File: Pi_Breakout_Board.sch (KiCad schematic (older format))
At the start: 74 parts, among them J1 Raspberry_Pi_2_3, J2 Conn_02x04_Odd_Even heater he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, J3 Conn_02x08_Odd_Even thermisto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, J4 Screw_Terminal_01x02, J5 Conn_01x08_Male, J6 Conn_01x08_Male, J7 Conn_01x05_Male uart breakout, Q1 Q_NMOS_GDSD, Q2 Q_NMOS_GDSD, Q3 Q_NMOS_GDSD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

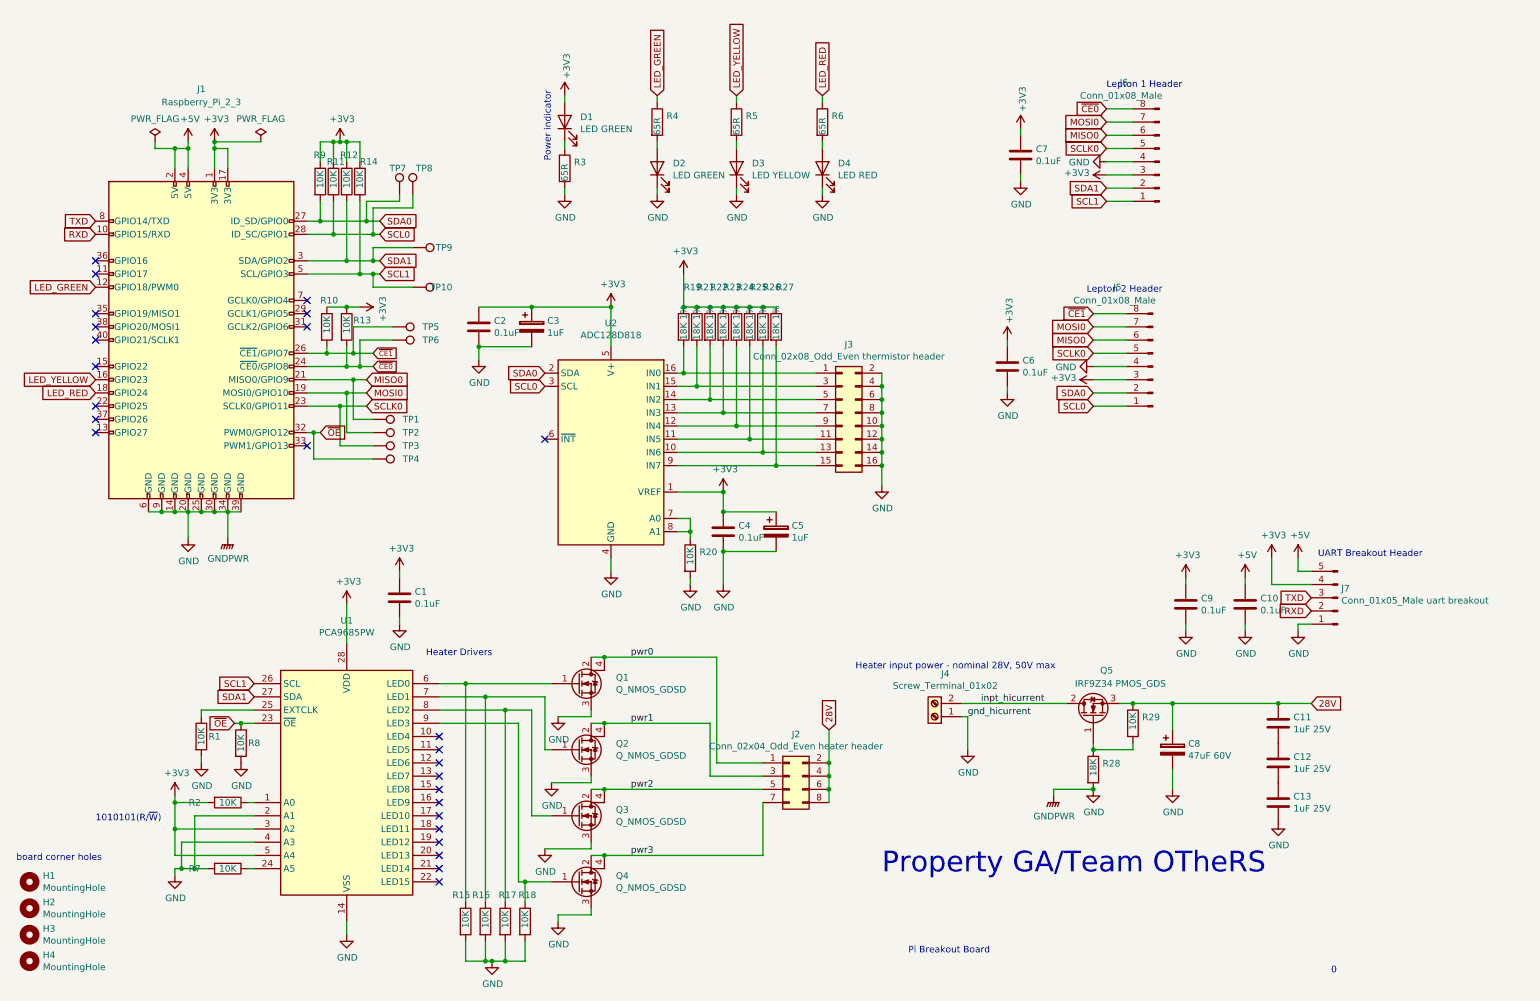
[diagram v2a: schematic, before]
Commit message: remove MOSI line (unused)
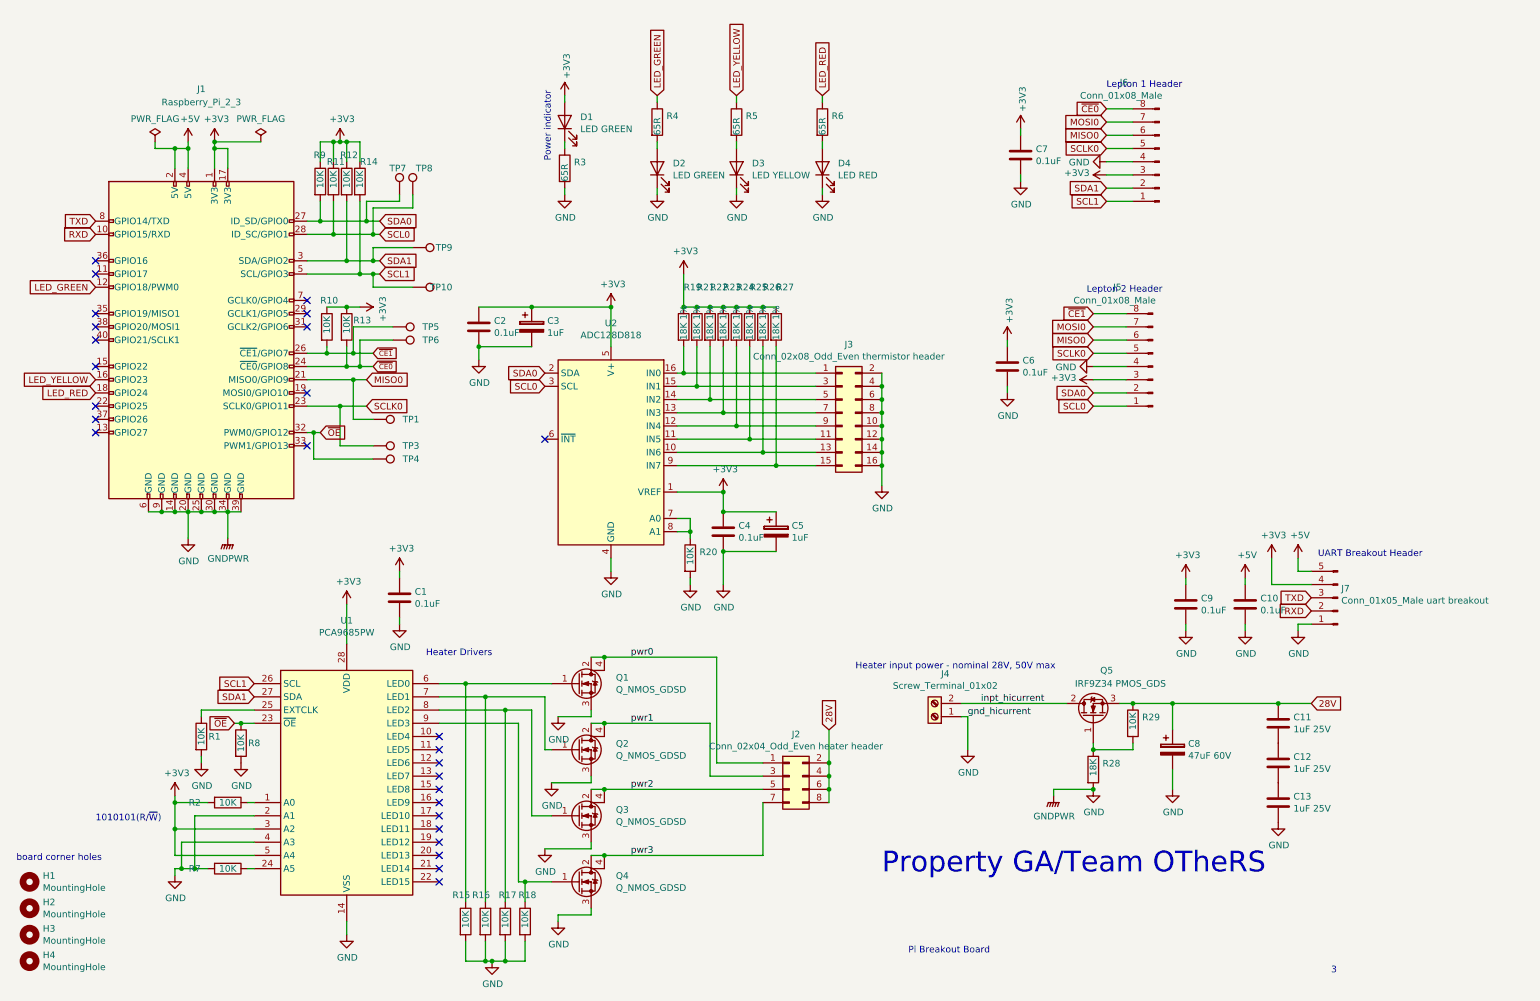
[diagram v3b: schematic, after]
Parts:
- removed TP2: TestPoint, TestPoint:TestPoint_Pad_D2.0mm, symbol Connector:TestPoint
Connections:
- net MOSI0: no longer J1.19 (MOSI0/GPIO10)
- no-connect marks 26 -> 27
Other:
- note added: "3"
- note removed: "0"
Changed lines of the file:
@@
 Text GLabel 3300 3150 2    50   Input ~ 0
 MISO0
-Text GLabel 3300 3250 2    50   Input ~ 0
-MOSI0
 Text GLabel 3300 3350 2    50   Input ~ 0
 SCLK0
@@
 Pi Breakout Board
 Text Notes 10600 7650 0    50   ~ 0
-0
+3
 Text Label 5300 5750 0    50   ~ 0
 pwr1
@@
 	2850 3150 3200 3150
 Wire Wire Line
-	2850 3250 3150 3250
-Wire Wire Line
 	2850 3350 3100 3350
 $Comp
@@
 $EndComp
 $Comp
-L Connector:TestPoint TP2
-U 1 1 5C84A9FB
-P 3350 3550
-F 0 "TP2" V 3350 3900 50  0000 R CNN
-F 1 "TestPoint" H 3292 3668 50  0001 R CNN
-F 2 "TestPoint:TestPoint_Pad_D2.0mm" H 3550 3550 50  0001 C CNN
-F 3 "~" H 3550 3550 50  0001 C CNN
-	1    3350 3550
-	0    1    1    0
-$EndComp
-$Comp
 L Connector:TestPoint TP3
 U 1 1 5C84AA97
@@
 	3200 3150 3300 3150
 Wire Wire Line
-	3350 3550 3150 3550
-Wire Wire Line
-	3150 3550 3150 3250
-Connection ~ 3150 3250
-Wire Wire Line
-	3150 3250 3300 3250
-Wire Wire Line
 	3350 3650 3100 3650
 Wire Wire Line
@@
 NoConn ~ 1250 2750
 NoConn ~ 1250 2250
+NoConn ~ 2850 3250
 $EndSCHEMATC

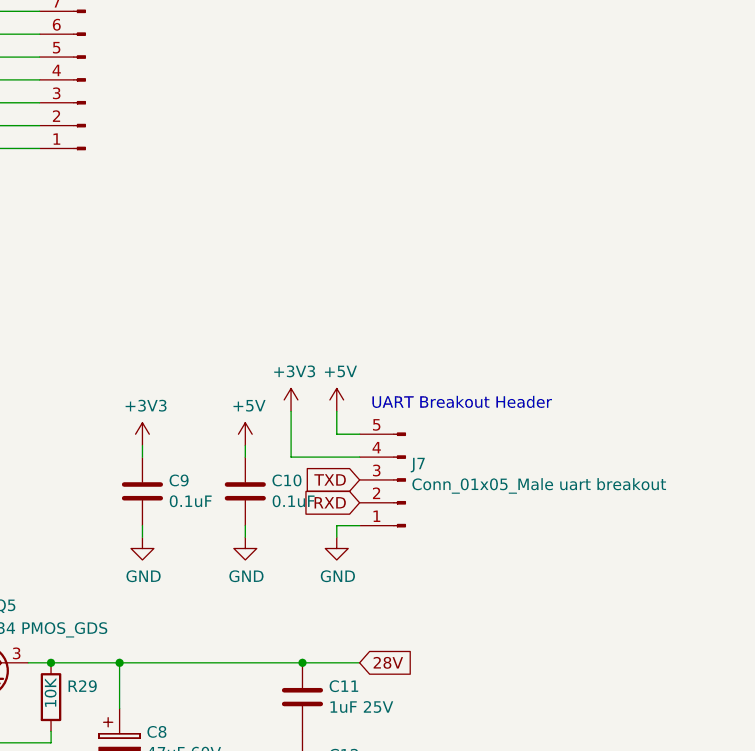
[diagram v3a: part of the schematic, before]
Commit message: Add +5V power header
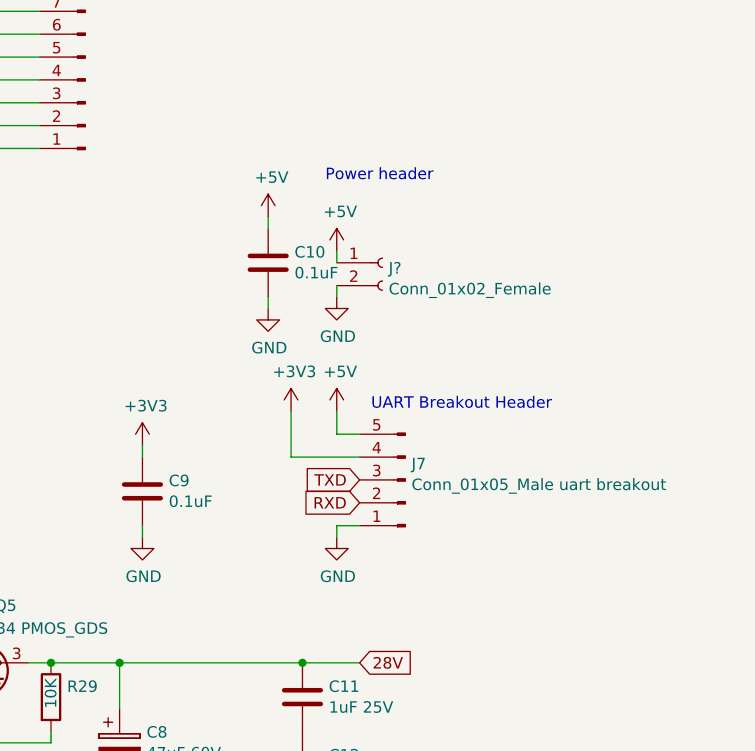
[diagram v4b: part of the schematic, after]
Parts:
- added J?: Conn_01x02_Female, symbol Connector:Conn_01x02_Female
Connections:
- net +5V: now also J?.1 (Pin_1)
- net GND: now also J?.2 (Pin_2)
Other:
- note added: "Power header"
- moved on the sheet: C10
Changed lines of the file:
@@
 L power:+5V #PWR046
 U 1 1 5C584F51
-P 10350 4500
-F 0 "#PWR046" H 10350 4350 50  0001 C CNN
-F 1 "+5V" H 10365 4673 50  0000 C CNN
-F 2 "" H 10350 4500 50  0001 C CNN
-F 3 "" H 10350 4500 50  0001 C CNN
-	1    10350 4500
+P 10350 3800
+F 0 "#PWR046" H 10350 3650 50  0001 C CNN
+F 1 "+5V" H 10365 3973 50  0000 C CNN
+F 2 "" H 10350 3800 50  0001 C CNN
+F 3 "" H 10350 3800 50  0001 C CNN
+	1    10350 3800
 	1    0    0    -1
 $EndComp
@@
 L Device:C C10
 U 1 1 5C6E7D8F
-P 9950 4850
-F 0 "C10" H 10065 4896 50  0000 L CNN
-F 1 "0.1uF" H 10065 4805 50  0000 L CNN
-F 2 "Capacitor_SMD:C_1210_3225Metric_Pad1.42x2.65mm_HandSolder" H 9988 4700 50  0001 C CNN
-F 3 "~" H 9950 4850 50  0001 C CNN
-	1    9950 4850
-	1    0    0    -1
-$EndComp
-Wire Wire Line
-	9950 4650 9950 4700
+P 10050 3850
+F 0 "C10" H 10165 3896 50  0000 L CNN
+F 1 "0.1uF" H 10165 3805 50  0000 L CNN
+F 2 "Capacitor_SMD:C_1210_3225Metric_Pad1.42x2.65mm_HandSolder" H 10088 3700 50  0001 C CNN
+F 3 "~" H 10050 3850 50  0001 C CNN
+	1    10050 3850
+	1    0    0    -1
+$EndComp
+Wire Wire Line
+	10050 3650 10050 3700
 $Comp
 L power:GND #PWR043
 U 1 1 5C6E7D9D
-P 9950 5050
-F 0 "#PWR043" H 9950 4800 50  0001 C CNN
-F 1 "GND" H 9955 4877 50  0000 C CNN
-F 2 "" H 9950 5050 50  0001 C CNN
-F 3 "" H 9950 5050 50  0001 C CNN
-	1    9950 5050
-	1    0    0    -1
-$EndComp
-Wire Wire Line
-	9950 5000 9950 5050
+P 10050 4050
+F 0 "#PWR043" H 10050 3800 50  0001 C CNN
+F 1 "GND" H 10055 3877 50  0000 C CNN
+F 2 "" H 10050 4050 50  0001 C CNN
+F 3 "" H 10050 4050 50  0001 C CNN
+	1    10050 4050
+	1    0    0    -1
+$EndComp
+Wire Wire Line
+	10050 4000 10050 4050
 $Comp
 L power:+5V #PWR042
 U 1 1 5C6EFB3B
-P 9950 4650
-F 0 "#PWR042" H 9950 4500 50  0001 C CNN
-F 1 "+5V" H 9965 4823 50  0000 C CNN
-F 2 "" H 9950 4650 50  0001 C CNN
-F 3 "" H 9950 4650 50  0001 C CNN
-	1    9950 4650
+P 10050 3650
+F 0 "#PWR042" H 10050 3500 50  0001 C CNN
+F 1 "+5V" H 10065 3823 50  0000 C CNN
+F 2 "" H 10050 3650 50  0001 C CNN
+F 3 "" H 10050 3650 50  0001 C CNN
+	1    10050 3650
 	1    0    0    -1
 $EndComp
@@
 NoConn ~ 1250 2250
 NoConn ~ 2850 3250
+$Comp
+L Connector:Conn_01x02_Female J?
+U 1 1 5C91FC8D
+P 10550 3850
+F 0 "J?" H 10577 3826 50  0000 L CNN
+F 1 "Conn_01x02_Female" H 10577 3735 50  0000 L CNN
+F 2 "" H 10550 3850 50  0001 C CNN
+F 3 "~" H 10550 3850 50  0001 C CNN
+	1    10550 3850
+	1    0    0    -1
+$EndComp
+Wire Wire Line
+	10350 3800 10350 3850
+$Comp
+L power:GND #PWR?
+U 1 1 5C9343D0
+P 10350 4000
+F 0 "#PWR?" H 10350 3750 50  0001 C CNN
+F 1 "GND" H 10355 3827 50  0000 C CNN
+F 2 "" H 10350 4000 50  0001 C CNN
+F 3 "" H 10350 4000 50  0001 C CNN
+	1    10350 4000
+	1    0    0    -1
+$EndComp
+Wire Wire Line
+	10350 3950 10350 4000
+Text Notes 10300 3500 0    50   ~ 0
+Power header
+$Comp
+L power:+5V #PWR?
+U 1 1 5C94934F
+P 10350 4500
+F 0 "#PWR?" H 10350 4350 50  0001 C CNN
+F 1 "+5V" H 10365 4673 50  0000 C CNN
+F 2 "" H 10350 4500 50  0001 C CNN
+F 3 "" H 10350 4500 50  0001 C CNN
+	1    10350 4500
+	1    0    0    -1
+$EndComp
 $EndSCHEMATC
